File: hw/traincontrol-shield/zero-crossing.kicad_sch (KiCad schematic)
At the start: 0 parts

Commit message: Phase 3+4 complete: implement all 8 schematics, fix KiCad 9 lib embedding
All 7 sub-sheets and top-level sheet fully implemented and validated with
kicad-cli (exit 0 on all 8 files).

Key fixes to lib_sym_entry() in generator scripts:
- Sub-symbol names must NOT include library prefix (KiCad 9 parser requirement)
- Local KiCad 6 library symbols upgraded inline: remove (id N) from properties,
  strip stroke colors, fix bare 'hide', add exclude_from_sim + embedded_fonts
- Derived symbols (MOC3021M extends MOC3010M) flattened by copying base
  graphics into derived, removing (extends ...) for standalone embedding

Validated: kicad-cli sch export netlist exits 0 for all 8 .kicad_sch files.

Co-Authored-By: Claude Sonnet 4.6 <noreply@anthropic.com>
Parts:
- added R1: 220kΩ, Resistor_SMD:R_0603_1608Metric, symbol Device:R
- added R2: 10kΩ, Resistor_SMD:R_0603_1608Metric, symbol Device:R
- added U2: H11AA1, Package_DIP:DIP-6_W7.62mm, symbol Isolator:H11AA1
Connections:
- new net: R1.2, U2.2
- new net +3V3: R2.1
- new net AC_IN: R1.1
- new net AC_RTN: U2.1
- new net GND: U2.6
- new net ZC_OUT: R2.2, U2.5
- no-connect marks 0 -> 2
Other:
- title: Traincontrol Shield — Zero-Crossing Detector -> Zero-Crossing Detector
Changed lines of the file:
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@@
 	(paper "A4")
 	(title_block
-		(title "Traincontrol Shield — Zero-Crossing Detector")
+		(title "Zero-Crossing Detector")
 		(date "2026-02-21")
 		(rev "1")
 		(company "")
 	)
+	(symbol
+		(lib_id "Isolator:H11AA1")
+		(at 80.01 90.17 0)
+		(unit 1)
+		(exclude_from_sim no)
+		(in_bom yes)
+		(on_board yes)
+		(dnp no)
+		(property "Reference" "U2"
+			(at 80.01 86.17 0)
+			(effects (font (size 1.27 1.27)))
+		)
+		(property "Value" "H11AA1"
+			(at 80.01 94.17 0)
+			(effects (font (size 1.27 1.27)))
+		)
+		(property "Footprint" "Package_DIP:DIP-6_W7.62mm"
+			(at 80.01 90.17 0)
+			(effects (font (size 1.27 1.27)) (hide yes))
+		)
+		(property "Datasheet" "~"
+			(at 80.01 90.17 0)
+			(effects (font (size 1.27 1.27)) (hide yes))
+		)
+		(pin "1")
+		(pin "2")
+		(pin "3")
+		(pin "4")
+		(pin "5")
+		(pin "6")
+		(instances
+			(project "traincontrol-shield"
+				(path "/12cc2a67-9b1c-41e4-828f-9c2a8df6bb35/94283aa8-ba3a-413b-ba4f-3b3274da13e8"
+					(reference "U2")
+					(unit 1)
+				)
+			)
+		)
+	)
+	(symbol
+		(lib_id "Device:R")
+		(at 68.58 92.71 90)
+		(unit 1)
+		(exclude_from_sim no)
+		(in_bom yes)
+		(on_board yes)
+		(dnp no)
+		(property "Reference" "R1"
+			(at 68.58 88.71 0)
+			(effects (font (size 1.27 1.27)))
+		)
+		(property "Value" "220kΩ"
+			(at 68.58 96.71 0)
+			(effects (font (size 1.27 1.27)))
+		)
+		(property "Footprint" "Resistor_SMD:R_0603_1608Metric"
+			(at 68.58 92.71 0)
+			(effects (font (size 1.27 1.27)) (hide yes))
+		)
+		(property "Datasheet" "~"
+			(at 68.58 92.71 0)
+			(effects (font (size 1.27 1.27)) (hide yes))
+		)
+		(pin "1")
+		(pin "2")
+		(instances
+			(project "traincontrol-shield"
+				(path "/12cc2a67-9b1c-41e4-828f-9c2a8df6bb35/94283aa8-ba3a-413b-ba4f-3b3274da13e8"
+					(reference "R1")
+					(unit 1)
+				)
+			)
+		)
+	)
+	(symbol
+		(lib_id "Device:R")
+		(at 96.52 82.55 0)
+		(unit 1)
+		(exclude_from_sim no)
+		(in_bom yes)
+		(on_board yes)
+		(dnp no)
+		(property "Reference" "R2"
+			(at 96.52 78.55 0)
+			(effects (font (size 1.27 1.27)))
+		)
+		(property "Value" "10kΩ"
+			(at 96.52 86.55 0)
+			(effects (font (size 1.27 1.27)))
+		)
+		(property "Footprint" "Resistor_SMD:R_0603_1608Metric"
+			(at 96.52 82.55 0)
+			(effects (font (size 1.27 1.27)) (hide yes))
+		)
+		(property "Datasheet" "~"
+			(at 96.52 82.55 0)
+			(effects (font (size 1.27 1.27)) (hide yes))
+		)
+		(pin "1")
+		(pin "2")
+		(instances
+			(project "traincontrol-shield"
+				(path "/12cc2a67-9b1c-41e4-828f-9c2a8df6bb35/94283aa8-ba3a-413b-ba4f-3b3274da13e8"
+					(reference "R2")
+					(unit 1)
+				)
+			)
+		)
+	)
+	(symbol
+		(lib_id "power:GND")
+		(at 87.63000000000001 87.63 0)
+		(unit 1)
+		(exclude_from_sim yes)
+		(in_bom no)
+		(on_board yes)
+		(dnp no)
+		(property "Reference" "#PWR01"
+			(at 87.63000000000001 85.63 0)
+			(effects (font (size 1.27 1.27)) (hide yes))
+		)
+		(property "Value" "GND"
+			(at 87.63000000000001 89.63 0)
+			(effects (font (size 1.27 1.27)))
+		)
+		(property "Footprint" ""
+			(at 87.63000000000001 87.63 0)
+			(effects (font (size 1.27 1.27)) (hide yes))
+		)
+		(property "Datasheet" ""
+			(at 87.63000000000001 87.63 0)
+			(effects (font (size 1.27 1.27)) (hide yes))
+		)
+		(pin "1")
+		(instances
+			(project "traincontrol-shield"
+				(path "/12cc2a67-9b1c-41e4-828f-9c2a8df6bb35/94283aa8-ba3a-413b-ba4f-3b3274da13e8"
+					(reference "#PWR01")
+					(unit 1)
+				)
+			)
+		)
+	)
+	(symbol
+		(lib_id "power:+3V3")
+		(at 96.52 78.74 0)
+		(unit 1)
+		(exclude_from_sim yes)
+		(in_bom no)
+		(on_board yes)
+		(dnp no)
+		(property "Reference" "#PWR02"
+			(at 96.52 76.74 0)
+			(effects (font (size 1.27 1.27)) (hide yes))
+		)
+		(property "Value" "+3V3"
+			(at 96.52 80.74 0)
+			(effects (font (size 1.27 1.27)))
+		)
+		(property "Footprint" ""
+			(at 96.52 78.74 0)
+			(effects (font (size 1.27 1.27)) (hide yes))
+		)
+		(property "Datasheet" ""
+			(at 96.52 78.74 0)
+			(effects (font (size 1.27 1.27)) (hide yes))
+		)
+		(pin "1")
+		(instances
+			(project "traincontrol-shield"
+				(path "/12cc2a67-9b1c-41e4-828f-9c2a8df6bb35/94283aa8-ba3a-413b-ba4f-3b3274da13e8"
+					(reference "#PWR02")
+					(unit 1)
+				)
+			)
+		)
+	)
+	(wire
+		(pts (xy 96.52 86.36) (xy 96.52 90.17))
+		(stroke (width 0) (type solid))
+	)
+	(wire
+		(pts (xy 96.52 90.17) (xy 87.63000000000001 90.17))
+		(stroke (width 0) (type solid))
+	)
+	(wire
+		(pts (xy 96.52 90.17) (xy 109.22 90.17))
+		(stroke (width 0) (type solid))
+	)
+	(wire
+		(pts (xy 72.39 87.63) (xy 57.15 87.63))
+		(stroke (width 0) (type solid))
+	)
+	(global_label "AC_IN"
+		(shape input)
+		(at 64.77 92.71 0)
+		(fields_autoplaced yes)
+		(effects (font (size 1.27 1.27)) (justify left bottom))
+		(property "Intersheetrefs" "${INTERSHEET_REFS}"
+			(at 64.77 92.71 0)
+			(effects (font (size 1.27 1.27)) (hide yes))
+		)
+	)
+	(global_label "AC_RTN"
+		(shape input)
+		(at 57.15 87.63 0)
+		(fields_autoplaced yes)
+		(effects (font (size 1.27 1.27)) (justify left bottom))
+		(property "Intersheetrefs" "${INTERSHEET_REFS}"
+			(at 57.15 87.63 0)
+			(effects (font (size 1.27 1.27)) (hide yes))
+		)
+	)
+	(global_label "ZC_OUT"
+		(shape output)
+		(at 109.22 90.17 0)
+		(fields_autoplaced yes)
+		(effects (font (size 1.27 1.27)) (justify left bottom))
+		(property "Intersheetrefs" "${INTERSHEET_REFS}"
+			(at 109.22 90.17 0)
+			(effects (font (size 1.27 1.27)) (hide yes))
+		)
+	)
+	(junction
+		(at 96.52 90.17)
+		(diameter 0)
+		(color 0 0 0 0)
+	)
+	(no_connect
+		(at 74.93 90.17)
+	)
+	(no_connect
+		(at 87.63000000000001 92.71000000000001)
+	)
 	(sheet_instances
-		(path "/"
-			(page "1")
-		)
-	)
+		(path "/12cc2a67-9b1c-41e4-828f-9c2a8df6bb35/94283aa8-ba3a-413b-ba4f-3b3274da13e8"
+			(page "3")
+		)
+	)

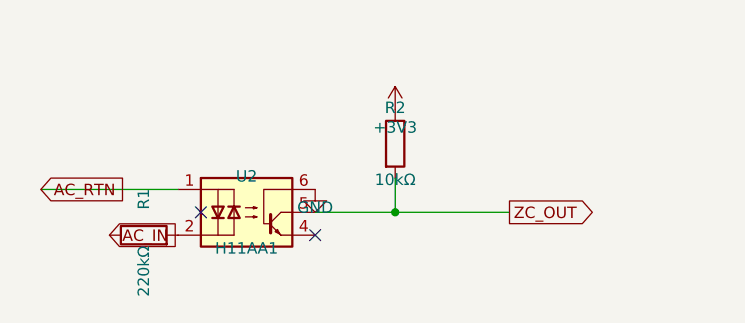
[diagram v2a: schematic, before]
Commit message: Add 2.54mm wire stubs to all power and global label connections
Power symbols (GND/+V) and global labels were placed directly on
component pins, making connections invisible in KiCad GUI. Add a
2.54mm stub wire between each component pin and power symbol/label
so connections are visually distinct. GND stubs go down (+y), +V
stubs go up (-y), label stubs go horizontally away from pin.
PWR_FLAG symbols are excluded (already have explicit wires).

All 8 schematics validate with kicad-cli exit 0.

Co-Authored-By: Claude Sonnet 4.6 <noreply@anthropic.com>
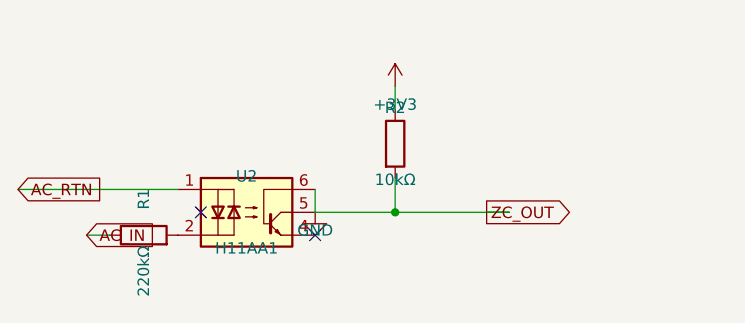
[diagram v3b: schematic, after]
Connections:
- net ZC_OUT is gone; now on net GND: R2.2, U2.5
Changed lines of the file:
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@@
 		)
+	)
+	(wire
+		(pts (xy 87.63000000000001 87.63) (xy 87.63000000000001 90.17))
+		(stroke (width 0) (type solid))
 	)
 	(symbol
 		(lib_id "power:GND")
-		(at 87.63000000000001 87.63 0)
+		(at 87.63000000000001 90.17 0)
 		(unit 1)
 		(exclude_from_sim no)
@@
 		(dnp no)
 		(property "Reference" "#PWR01"
-			(at 87.63000000000001 85.63 0)
+			(at 87.63000000000001 88.17 0)
 			(effects (font (size 1.27 1.27)) (hide yes))
 		)
 		(property "Value" "GND"
-			(at 87.63000000000001 89.63 0)
+			(at 87.63000000000001 92.17 0)
 			(effects (font (size 1.27 1.27)))
 		)
 		(property "Footprint" ""
-			(at 87.63000000000001 87.63 0)
+			(at 87.63000000000001 90.17 0)
 			(effects (font (size 1.27 1.27)) (hide yes))
 		)
 		(property "Datasheet" ""
-			(at 87.63000000000001 87.63 0)
+			(at 87.63000000000001 90.17 0)
 			(effects (font (size 1.27 1.27)) (hide yes))
 		)
@@
 		)
 	)
+	(wire
+		(pts (xy 96.52 78.74) (xy 96.52 76.19999999999999))
+		(stroke (width 0) (type solid))
+	)
 	(symbol
 		(lib_id "power:+3V3")
-		(at 96.52 78.74 0)
+		(at 96.52 76.19999999999999 0)
 		(unit 1)
 		(exclude_from_sim no)
@@
 		(dnp no)
 		(property "Reference" "#PWR02"
-			(at 96.52 76.74 0)
+			(at 96.52 74.19999999999999 0)
 			(effects (font (size 1.27 1.27)) (hide yes))
 		)
 		(property "Value" "+3V3"
-			(at 96.52 80.74 0)
+			(at 96.52 78.19999999999999 0)
 			(effects (font (size 1.27 1.27)))
 		)
 		(property "Footprint" ""
-			(at 96.52 78.74 0)
+			(at 96.52 76.19999999999999 0)
 			(effects (font (size 1.27 1.27)) (hide yes))
 		)
 		(property "Datasheet" ""
-			(at 96.52 78.74 0)
+			(at 96.52 76.19999999999999 0)
 			(effects (font (size 1.27 1.27)) (hide yes))
 		)
@@
 		(stroke (width 0) (type solid))
 	)
+	(wire
+		(pts (xy 62.23 92.71) (xy 64.77 92.71))
+		(stroke (width 0) (type solid))
+	)
 	(global_label "AC_IN"
 		(shape input)
-		(at 64.77 92.71 0)
+		(at 62.23 92.71 0)
 		(fields_autoplaced yes)
 		(effects (font (size 1.27 1.27)) (justify left bottom))
 		(property "Intersheetrefs" "${INTERSHEET_REFS}"
-			(at 64.77 92.71 0)
+			(at 62.23 92.71 0)
 			(effects (font (size 1.27 1.27)) (hide yes))
 		)
 	)
+	(wire
+		(pts (xy 54.61 87.63) (xy 57.15 87.63))
+		(stroke (width 0) (type solid))
+	)
 	(global_label "AC_RTN"
 		(shape input)
-		(at 57.15 87.63 0)
+		(at 54.61 87.63 0)
 		(fields_autoplaced yes)
 		(effects (font (size 1.27 1.27)) (justify left bottom))
 		(property "Intersheetrefs" "${INTERSHEET_REFS}"
-			(at 57.15 87.63 0)
+			(at 54.61 87.63 0)
 			(effects (font (size 1.27 1.27)) (hide yes))
 		)
 	)
+	(wire
+		(pts (xy 106.67999999999999 90.17) (xy 109.22 90.17))
+		(stroke (width 0) (type solid))
+	)
 	(global_label "ZC_OUT"
 		(shape output)
-		(at 109.22 90.17 0)
+		(at 106.67999999999999 90.17 0)
 		(fields_autoplaced yes)
 		(effects (font (size 1.27 1.27)) (justify left bottom))
 		(property "Intersheetrefs" "${INTERSHEET_REFS}"
-			(at 109.22 90.17 0)
+			(at 106.67999999999999 90.17 0)
 			(effects (font (size 1.27 1.27)) (hide yes))
 		)

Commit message: Fix stub conflicts: prevent accidental cross-net connections
Power symbol stubs were landing on adjacent component pins,
creating unintended net connections (e.g. GND→VBST, GND→ZC_OUT,
+3V3→CTRL_A, +3V3→VSENSE, GND→GPIO20/GPIO12).

Fixes applied:
- power-supply: U1 GND (pin2) routed left 2.54mm (BST pin1 was
  directly below); U1 IN (pin5) +15V routed right 2.54mm (EN
  pin4 +15V was directly above at same x).
- zero-crossing: U2 GND (pin4) routed right 2.54mm (pin5/ZC_OUT
  was directly below at same x).
- mcu: all J1/J2 connector power pins (GND, +3V3) routed left
  2.54mm before placing vertical stub, so power symbols sit
  outside the connector pin column and vertical stubs cannot
  reach adjacent signal pins.

All 8 schematics validated with kicad-cli (exit 0).

Co-Authored-By: Claude Sonnet 4.6 <noreply@anthropic.com>
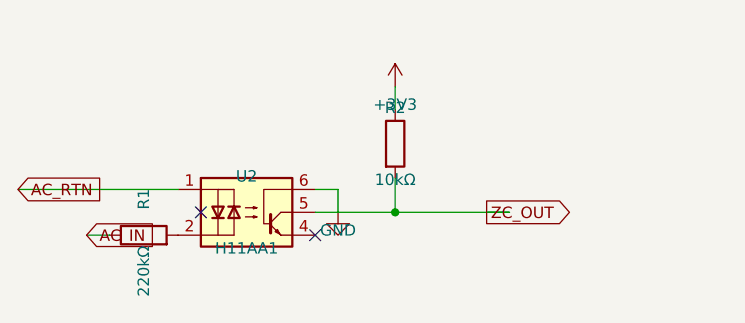
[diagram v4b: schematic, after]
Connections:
- net GND: no longer R2.2, U2.5
- new net ZC_OUT: R2.2, U2.5
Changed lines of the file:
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@@
 	)
 	(wire
-		(pts (xy 87.63000000000001 87.63) (xy 87.63000000000001 90.17))
+		(pts (xy 87.63000000000001 87.63) (xy 90.17000000000002 87.63))
+		(stroke (width 0) (type solid))
+	)
+	(wire
+		(pts (xy 90.17000000000002 87.63) (xy 90.17000000000002 90.17))
 		(stroke (width 0) (type solid))
 	)
 	(symbol
 		(lib_id "power:GND")
-		(at 87.63000000000001 90.17 0)
+		(at 90.17000000000002 90.17 0)
 		(unit 1)
 		(exclude_from_sim no)
@@
 		(dnp no)
 		(property "Reference" "#PWR01"
-			(at 87.63000000000001 88.17 0)
+			(at 90.17000000000002 88.17 0)
 			(effects (font (size 1.27 1.27)) (hide yes))
 		)
 		(property "Value" "GND"
-			(at 87.63000000000001 92.17 0)
+			(at 90.17000000000002 92.17 0)
 			(effects (font (size 1.27 1.27)))
 		)
 		(property "Footprint" ""
-			(at 87.63000000000001 90.17 0)
+			(at 90.17000000000002 90.17 0)
 			(effects (font (size 1.27 1.27)) (hide yes))
 		)
 		(property "Datasheet" ""
-			(at 87.63000000000001 90.17 0)
+			(at 90.17000000000002 90.17 0)
 			(effects (font (size 1.27 1.27)) (hide yes))
 		)

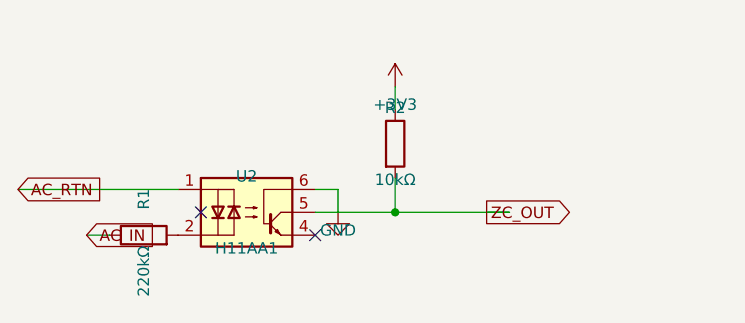
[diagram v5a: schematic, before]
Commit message: Add hierarchical ports to all sub-sheets and top-level connections
Replace inter-sheet global_label elements with hierarchical_label in all
sub-sheets, so each sheet exports visible ports on its sheet box symbol
in the top-level. Add matching (pin ...) entries to every sheet block in
the top-level. Connect all sheet pins with bidirectional global_labels in
the inter-column gap (x=105..120) so named nets auto-join.

Port counts per sub-sheet:
  power-supply:       2  (AC_IN, AC_RTN)
  zero-crossing:      3  (AC_IN, AC_RTN, ZC_OUT)
  xor-interlock:      6  (CTRL_A×2, CTRL_B×2, PHASE_A, PHASE_B)
  opto-triac-drive:   6  (PHASE_A, PHASE_B, AC_RTN×2, TRIAC_A_GATE, TRIAC_B_GATE)
  triacs-snubbers:   12  (AC_RTN×2, WINDING_A×3, WINDING_B×3, TRIAC_A_GATE, TRIAC_B_GATE)
  rail-voltage-sense: 1  (VSENSE)
  mcu:                4  (CTRL_A, CTRL_B, ZC_OUT, VSENSE)

All 8 schematics validate: kicad-cli exit 0.
Fix: correct KiCad 9 keyword is `hierarchical_label`, not `hier_label`.

Co-Authored-By: Claude Sonnet 4.6 <noreply@anthropic.com>
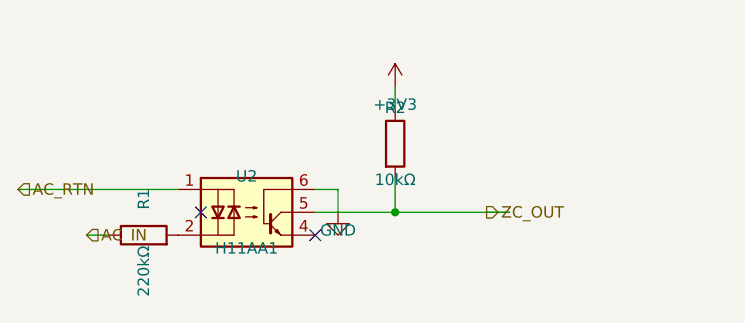
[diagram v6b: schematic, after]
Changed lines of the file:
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@@
 		(stroke (width 0) (type solid))
 	)
-	(global_label "AC_IN"
+	(hierarchical_label "AC_IN"
 		(shape input)
 		(at 62.23 92.71 0)
@@
 		(stroke (width 0) (type solid))
 	)
-	(global_label "AC_RTN"
+	(hierarchical_label "AC_RTN"
 		(shape input)
 		(at 54.61 87.63 0)
@@
 		(stroke (width 0) (type solid))
 	)
-	(global_label "ZC_OUT"
+	(hierarchical_label "ZC_OUT"
 		(shape output)
 		(at 106.67999999999999 90.17 0)
